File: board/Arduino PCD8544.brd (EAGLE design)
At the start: 49.2 x 72.4 mm, 30 parts, among them IC1 ATMEGA328-20P, IC2 REG1117, Y1 8/16MHz

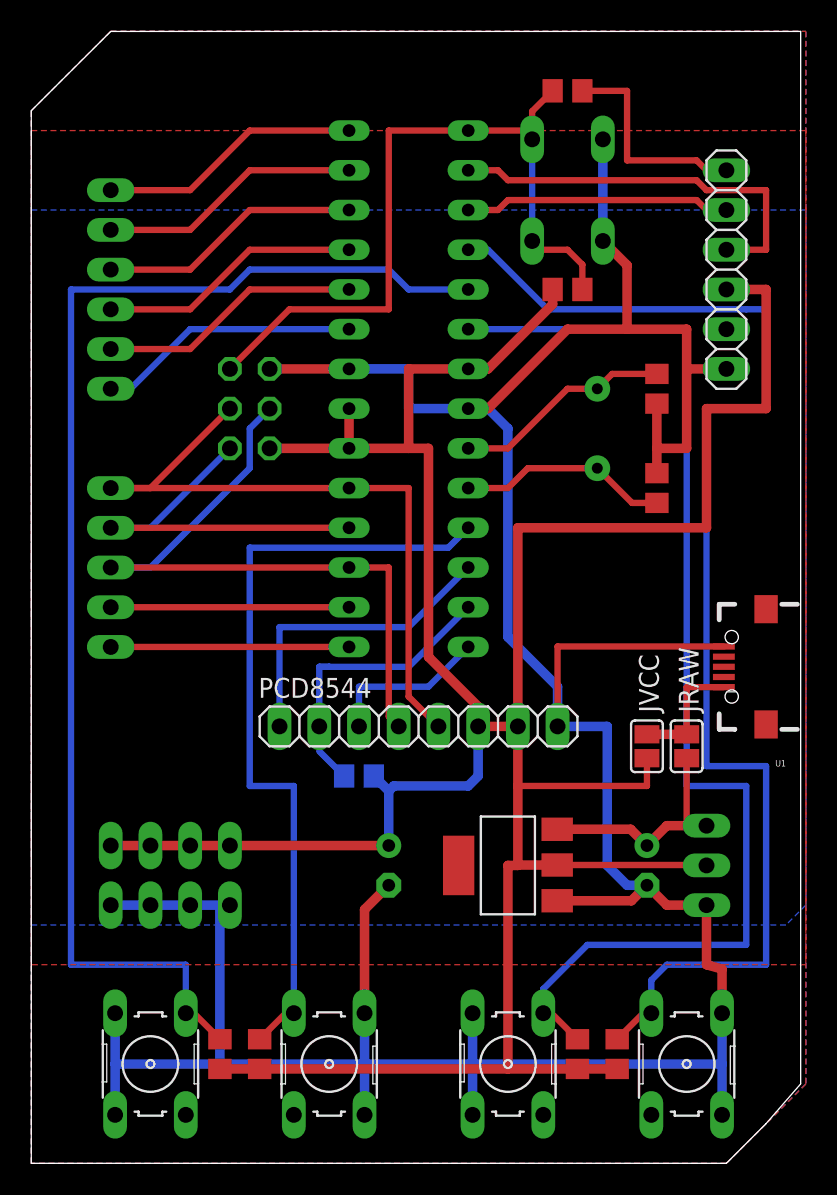
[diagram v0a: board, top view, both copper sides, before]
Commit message: Updated board
* Moved push button and power positions
* Moved µUSB to bottom centre of board
* Added mounting holes to suit https://evatron.com/enclosures/oval-enclosures/sb107g/
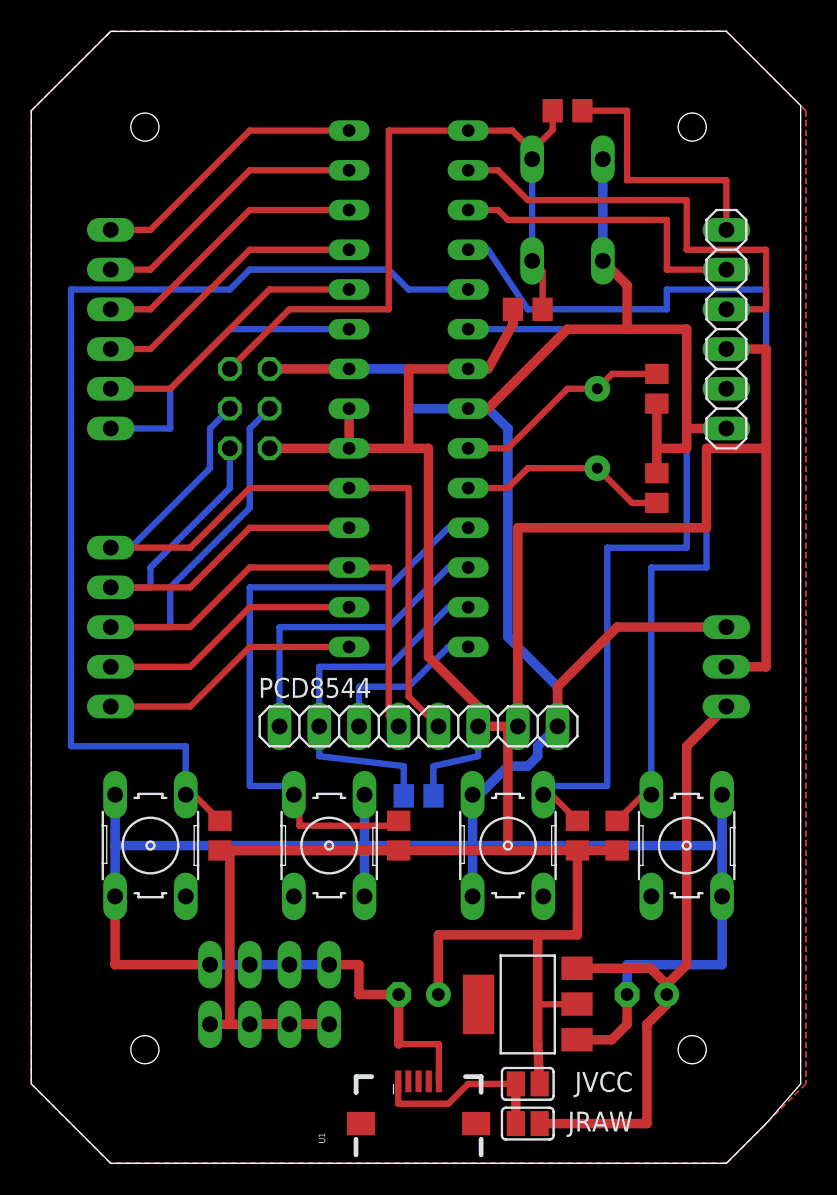
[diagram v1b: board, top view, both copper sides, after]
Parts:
- moved U1 36.7 mm to (24.8, 2.54), turned to 90 degrees
- moved JRAW 26.2 mm to (31.8, 2.54), turned to 180 degrees
- moved JVCC 22.9 mm to (31.8, 5.08), turned to 180 degrees
- moved R2 16.6 mm to (23.5, 21.0)
- moved S2 14.0 mm to (30.5, 20.3)
- moved S3 14.0 mm to (41.9, 20.3)
- moved S4 14.0 mm to (19.1, 20.3)
- moved S5 14.0 mm to (7.62, 20.3)
- moved R3 14.0 mm to (34.9, 21.0)
- moved R4 14.0 mm to (37.5, 21.0)
- moved R5 14.0 mm to (12.1, 21.0)
- moved VCC 13.1 mm to (15.2, 8.89)
- moved PWR 12.8 mm to (44.5, 31.8), turned to 270 degrees
- moved IC2 8.98 mm to (31.8, 10.2)
- moved C8 8.47 mm to (24.8, 10.8), turned to 0 degrees
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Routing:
- net RAW: track 14.8 -> 41.8 mm
- net UP: track 75.7 -> 57.2 mm
- net OK: track 82.9 -> 64.9 mm
- net CANCEL: track 82.9 -> 69.0 mm
- net VCC: track 199.6 -> 212.7 mm
- net DOWN: track 50.0 -> 40.6 mm
- net LCD_CS: track 17.8 -> 24.2 mm
- net MOSI: track 45.3 -> 50.2 mm
- net SCK: track 44.8 -> 49.4 mm
- net GND: track 225.1 -> 220.9 mm
- net MISO: track 26.2 -> 30.4 mm
- net N$1: track 7.94 -> 12.0 mm
- net 0/RX: track 25.9 -> 29.4 mm
- net DTR: track 13.9 -> 16.8 mm
- net 1/TX: track 17.0 -> 19.9 mm
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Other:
- outline, holes or cut-outs redrawn
- board text added: "GND VCC RAW"
- board text removed: "RAW VCC GND"
